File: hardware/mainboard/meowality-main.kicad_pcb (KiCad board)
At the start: 6 copper layers, 200 x 75 mm, 266 parts, among them J1 Micro_SD_Card_Det, J2 MINI_DP_SINK, J3 DEBUG, J4 USB_C_Receptacle, J5 Conn_01x02, J6 Conn_01x02, P1 M2_SOCKET_E, Q1 BSS138, Q10 BSS138, Q2 BSS138, Q3 BSS138, Q5 BSS138, Q7 BSS138, SW1 SW_DIP_x04, SW2 SW_Push, SW3 SW_Push, SW4 SW_Push, SW5 SW_Push, SW6 SW_Push, U1 CP3225-100.000-3.3-25-X-T-TR, U10 MMC5983MA, U11 Si52112-B, U12 TPD4E02B04DQA, U13 TPD4E02B04DQA, U14 CBTL02043A, U15 FUSB302B11MPX, U16 USB3318, U17 AP6230xWU, U19 ADP5070ACPZ, U2 AX3HAF1-135.0000T, U20 CAT4106HV4, U21 74LVC2T45DC, U3 AP6230xWU, U4 AP6230xWU, U5 SiC438, U6 AP6230xWU, U7 AP6230xWU, U8 TXS02612, U9 ICM-20789, X1 831056169, Y1 25MHz

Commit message: Fix LCD connector rotation
Signed-off-by: gatecat <gatecat@ds0.me>
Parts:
- turned LCD1 to 90 degrees
- turned LCD2 to 90 degrees

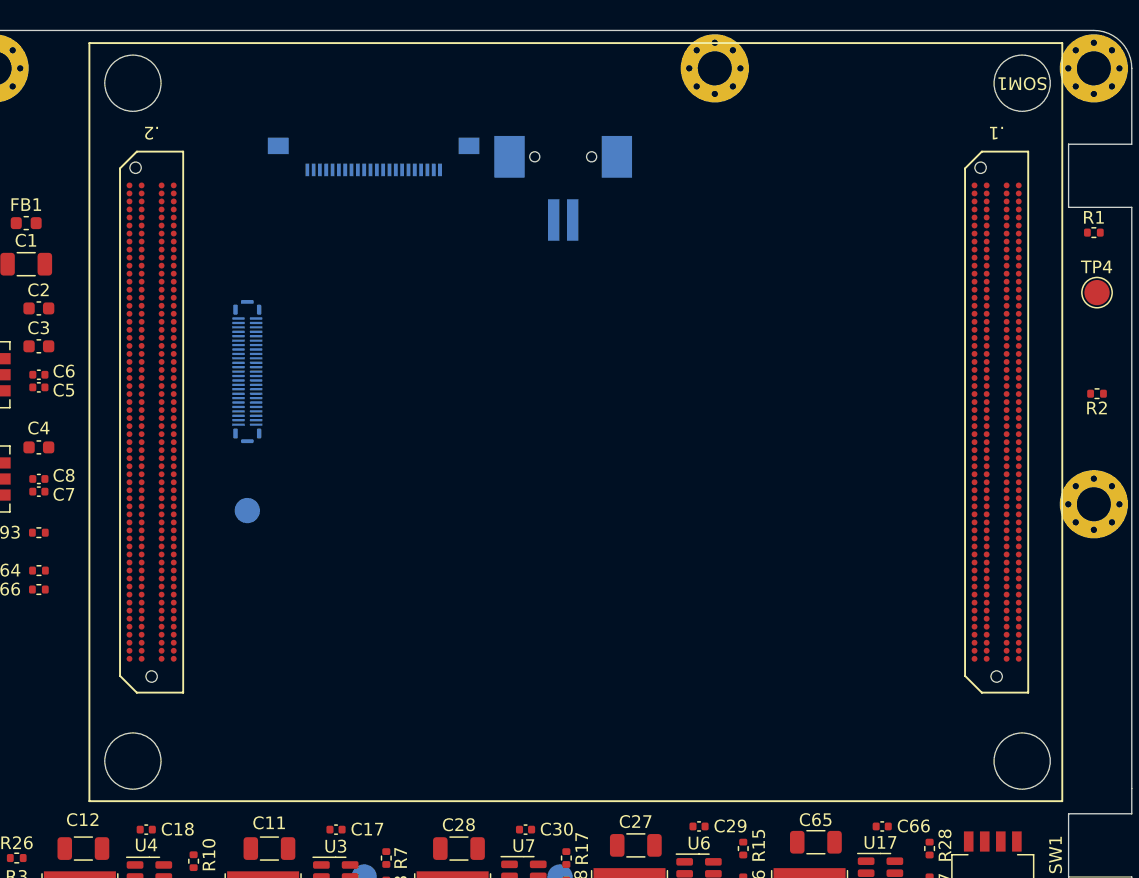
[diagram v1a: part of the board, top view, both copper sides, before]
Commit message: Minor layout changes
Signed-off-by: gatecat <gatecat@ds0.me>
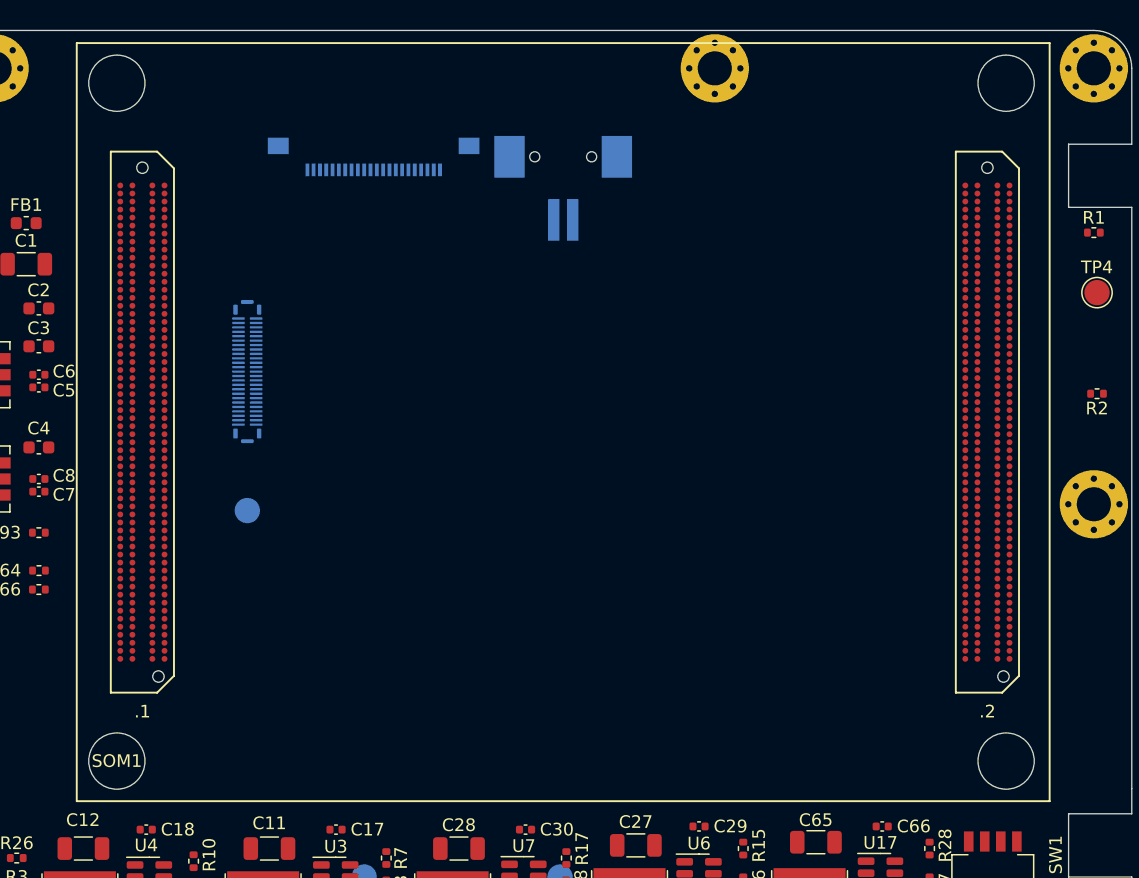
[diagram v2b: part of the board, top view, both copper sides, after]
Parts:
- moved SOM1 89.5 mm to (149.7, 117.8), turned to 0 degrees

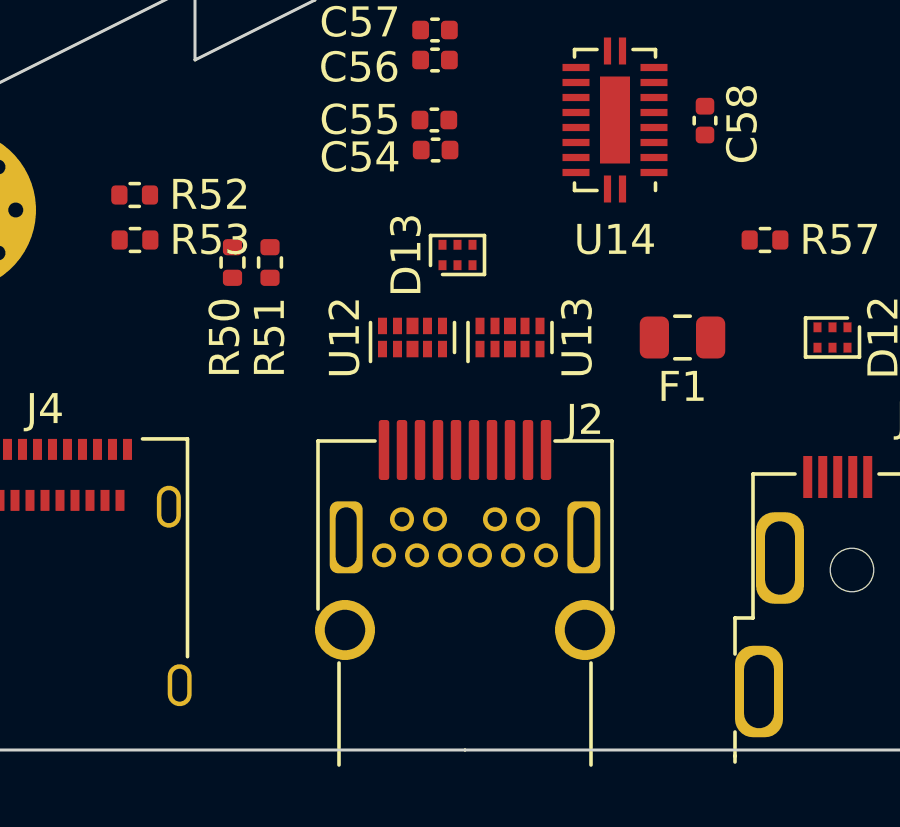
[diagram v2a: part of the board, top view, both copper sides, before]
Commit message: Alternate DP connector
Signed-off-by: gatecat <gatecat@ds0.me>
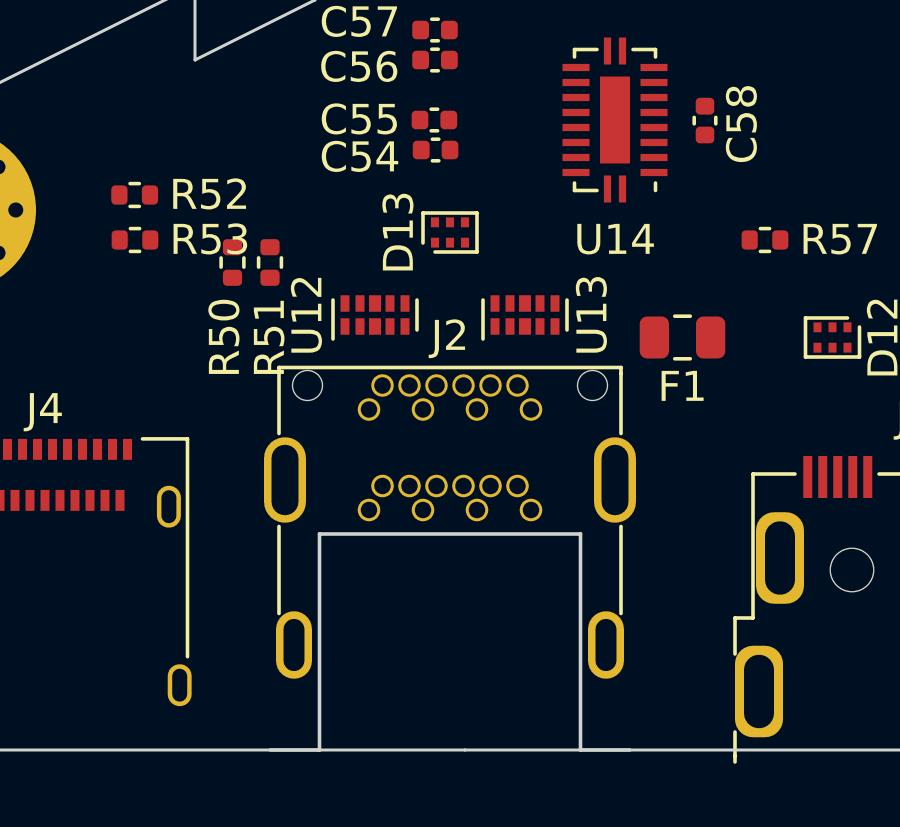
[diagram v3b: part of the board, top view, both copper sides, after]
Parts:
- J2: footprint meowality:E9320-001-01 -> meowality:2129320-3
- moved J2 8.17 mm to (49.5, 122.8), turned to 0 degrees
- moved U12 1.46 mm to (47.0, 120.5)
- moved U13 0.90 mm to (52.0, 120.5)
- moved D13 0.79 mm to (49.5, 117.8)
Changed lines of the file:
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@@
     )
   )
-  (footprint "meowality:E9320-001-01" (layer "F.Cu")
-    (at 50 131 180)
+  (footprint "meowality:2129320-3" (layer "F.Cu")
+    (at 49.5 122.85)
     (property "Sheetfile" "io.kicad_sch")
     (property "Sheetname" "IO")
-    (attr smd)
-    (fp_text reference "J2" (at -4 7 unlocked) (layer "F.SilkS")
+    (attr through_hole)
+    (fp_text reference "J2" (at 0 -1.65 unlocked) (layer "F.SilkS")
       (effects (font (size 1 1) (thickness 0.15)))
     )
-    (fp_text value "MINI_DP_SINK" (at 0 1 180 unlocked) (layer "F.Fab")
+    (fp_text value "MINI_DP_SINK" (at 0 3.75 unlocked) (layer "F.Fab")
       (effects (font (size 1 1) (thickness 0.15)))
     )
-    (fp_text user "${REFERENCE}" (at 0 2.5 180 unlocked) (layer "F.Fab")
+    (fp_text user "${REFERENCE}" (at 0 2.5 unlocked) (layer "F.Fab")
       (effects (font (size 1 1) (thickness 0.15)))
     )
-    (fp_line (start 4.9 6.3) (end 4.9 0.7) (layer "F.SilkS") (width 0.12))
-    (fp_line (start -4.9 6.3) (end -3 6.3) (layer "F.SilkS") (width 0.12))
-    (fp_line (start -4.2 -1.1) (end -4.2 -4.5) (layer "F.SilkS") (width 0.12))
-    (fp_line (start -4.9 0.7) (end -4.9 6.3) (layer "F.SilkS") (width 0.12))
-    (fp_line (start 4.2 -4.5) (end 4.2 -1.1) (layer "F.SilkS") (width 0.12))
-    (fp_line (start 3 6.3) (end 4.9 6.3) (layer "F.SilkS") (width 0.12))
-    (fp_line (start 0 -4.5) (end 4.2 -4.5) (layer "Eco1.User") (width 0.12))
-    (fp_line (start 0 -4.5) (end -4.2 -4.5) (layer "Eco1.User") (width 0.12))
-    (pad "1" smd roundrect (at 2.7 6 180) (size 0.35 2) (layers "F.Cu" "F.Paste" "F.Mask") (roundrect_rratio 0.25)
+    (fp_line (start 5.7 -0.4) (end 5.7 1.6) (layer "F.SilkS") (width 0.12))
+    (fp_line (start 5.7 -0.6) (end -5.7 -0.6) (layer "F.SilkS") (width 0.12))
+    (fp_line (start -5.7 -0.6) (end -5.7 1.6) (layer "F.SilkS") (width 0.12))
+    (fp_line (start 5.7 -0.4) (end 5.7 -0.6) (layer "F.SilkS") (width 0.12))
+    (fp_line (start 5.7 4.7) (end 5.7 7.6) (layer "F.SilkS") (width 0.12))
+    (fp_line (start -5.7 4.7) (end -5.7 7.6) (layer "F.SilkS") (width 0.12))
+    (fp_line (start 4.35 4.95) (end -4.35 4.95) (layer "Edge.Cuts") (width 0.12))
+    (fp_line (start 4.35 12.15) (end 6 12.15) (layer "Edge.Cuts") (width 0.12))
+    (fp_line (start -4.35 4.95) (end -4.35 12.15) (layer "Edge.Cuts") (width 0.12))
+    (fp_line (start 4.35 12.15) (end 4.35 4.95) (layer "Edge.Cuts") (width 0.12))
+    (fp_line (start -4.35 12.15) (end -6 12.15) (layer "Edge.Cuts") (width 0.12))
+    (pad "" np_thru_hole circle (at -4.75 0) (size 1 1) (drill 1) (layers F&B.Cu *.Mask))
+    (pad "" np_thru_hole circle (at 4.75 0) (size 1 1) (drill 1) (layers F&B.Cu *.Mask))
+    (pad "1" thru_hole circle (at -2.7 4.15) (size 0.75 0.75) (drill 0.55) (layers *.Cu *.Mask)
       (net 2 "GND") (pinfunction "GND") (pintype "passive"))
-    (pad "2" thru_hole circle (at 2.7 2.49 180) (size 0.8 0.8) (drill 0.5) (layers *.Cu "B.Mask")
+    (pad "2" thru_hole circle (at -2.7 0.8) (size 0.75 0.75) (drill 0.55) (layers *.Cu *.Mask)
       (net 111 "DP_HPD") (pinfunction "HPD") (pintype "passive"))
-    (pad "3" smd roundrect (at 2.1 6 180) (size 0.35 2) (layers "F.Cu" "F.Paste" "F.Mask") (roundrect_rratio 0.25)
+    (pad "3" thru_hole circle (at -2.25 3.35) (size 0.75 0.75) (drill 0.55) (layers *.Cu *.Mask)
       (net 129 "DP_IN_L3-") (pinfunction "ML_L3-") (pintype "passive"))
-    (pad "4" thru_hole circle (at 2.1 3.69 180) (size 0.8 0.8) (drill 0.5) (layers *.Cu "B.Mask")
+    (pad "4" thru_hole circle (at -2.25 0) (size 0.75 0.75) (drill 0.55) (layers *.Cu *.Mask)
       (net 130 "Net-(J2-Pad4)") (pinfunction "CONFIG1") (pintype "passive"))
-    (pad "5" smd roundrect (at 1.5 6 180) (size 0.35 2) (layers "F.Cu" "F.Paste" "F.Mask") (roundrect_rratio 0.25)
+    (pad "5" thru_hole circle (at -1.35 3.35) (size 0.75 0.75) (drill 0.55) (layers *.Cu *.Mask)
       (net 131 "DP_IN_L3+") (pinfunction "ML_L3+") (pintype "passive"))
-    (pad "6" thru_hole circle (at 1.6 2.49 180) (size 0.8 0.8) (drill 0.5) (layers *.Cu "B.Mask")
+    (pad "6" thru_hole circle (at -1.35 0) (size 0.75 0.75) (drill 0.55) (layers *.Cu *.Mask)
       (net 132 "Net-(J2-Pad6)") (pinfunction "CONFIG2") (pintype "passive"))
-    (pad "7" smd roundrect (at 0.9 6 180) (size 0.35 2) (layers "F.Cu" "F.Paste" "F.Mask") (roundrect_rratio 0.25)
+    (pad "7" thru_hole circle (at -0.9 4.15) (size 0.75 0.75) (drill 0.55) (layers *.Cu *.Mask)
       (net 2 "GND") (pinfunction "GND") (pintype "passive"))
-    (pad "8" thru_hole circle (at 1 3.69 180) (size 0.8 0.8) (drill 0.5) (layers *.Cu "B.Mask")
+    (pad "8" thru_hole circle (at -0.9 0.8) (size 0.75 0.75) (drill 0.55) (layers *.Cu *.Mask)
       (net 2 "GND") (pinfunction "GND") (pintype "passive"))
-    (pad "9" smd roundrect (at 0.3 6 180) (size 0.35 2) (layers "F.Cu" "F.Paste" "F.Mask") (roundrect_rratio 0.25)
+    (pad "9" thru_hole circle (at -0.45 3.35) (size 0.75 0.75) (drill 0.55) (layers *.Cu *.Mask)
       (net 133 "DP_IN_L2-") (pinfunction "ML_L2-") (pintype "passive"))
-    (pad "10" thru_hole circle (at 0.5 2.49 180) (size 0.8 0.8) (drill 0.5) (layers *.Cu "B.Mask")
+    (pad "10" thru_hole circle (at -0.45 0) (size 0.75 0.75) (drill 0.55) (layers *.Cu *.Mask)
       (net 134 "DP_IN_L0-") (pinfunction "ML_L0-") (pintype "passive"))
-    (pad "11" smd roundrect (at -0.3 6 180) (size 0.35 2) (layers "F.Cu" "F.Paste" "F.Mask") (roundrect_rratio 0.25)
+    (pad "11" thru_hole circle (at 0.45 3.35) (size 0.75 0.75) (drill 0.55) (layers *.Cu *.Mask)
       (net 135 "DP_IN_L2+") (pinfunction "ML_L2+") (pintype "passive"))
-    (pad "12" thru_hole circle (at -0.5 2.49 180) (size 0.8 0.8) (drill 0.5) (layers *.Cu "B.Mask")
+    (pad "12" thru_hole circle (at 0.45 0) (size 0.75 0.75) (drill 0.55) (layers *.Cu *.Mask)
       (net 136 "DP_IN_L0+") (pinfunction "ML_L0+") (pintype "passive"))
-    (pad "13" smd roundrect (at -0.9 6 180) (size 0.35 2) (layers "F.Cu" "F.Paste" "F.Mask") (roundrect_rratio 0.25)
+    (pad "13" thru_hole circle (at 0.9 4.15) (size 0.75 0.75) (drill 0.55) (layers *.Cu *.Mask)
       (net 2 "GND") (pinfunction "GND") (pintype "passive"))
-    (pad "14" thru_hole circle (at -1 3.69 180) (size 0.8 0.8) (drill 0.5) (layers *.Cu "B.Mask")
+    (pad "14" thru_hole circle (at 0.9 0.8) (size 0.75 0.75) (drill 0.55) (layers *.Cu *.Mask)
       (net 2 "GND") (pinfunction "GND") (pintype "passive"))
-    (pad "15" smd roundrect (at -1.5 6 180) (size 0.35 2) (layers "F.Cu" "F.Paste" "F.Mask") (roundrect_rratio 0.25)
+    (pad "15" thru_hole circle (at 1.35 3.35) (size 0.75 0.75) (drill 0.55) (layers *.Cu *.Mask)
       (net 137 "DP_IN_L1-") (pinfunction "ML_L1-") (pintype "passive"))
-    (pad "16" thru_hole circle (at -1.6 2.49 180) (size 0.8 0.8) (drill 0.5) (layers *.Cu "B.Mask")
+    (pad "16" thru_hole circle (at 1.35 0) (size 0.75 0.75) (drill 0.55) (layers *.Cu *.Mask)
       (net 112 "DP_AUX+") (pinfunction "AUX+") (pintype "passive"))
-    (pad "17" smd roundrect (at -2.1 6 180) (size 0.35 2) (layers "F.Cu" "F.Paste" "F.Mask") (roundrect_rratio 0.25)
+    (pad "17" thru_hole circle (at 2.25 3.35) (size 0.75 0.75) (drill 0.55) (layers *.Cu *.Mask)
       (net 138 "DP_IN_L1+") (pinfunction "ML_L1+") (pintype "passive"))
-    (pad "18" thru_hole circle (at -2.1 3.69 180) (size 0.8 0.8) (drill 0.5) (layers *.Cu *.Mask)
+    (pad "18" thru_hole circle (at 2.25 0) (size 0.75 0.75) (drill 0.55) (layers *.Cu *.Mask)
       (net 113 "DP_AUX-") (pinfunction "AUX-") (pintype "passive"))
-    (pad "19" smd roundrect (at -2.7 6 180) (size 0.35 2) (layers "F.Cu" "F.Paste" "F.Mask") (roundrect_rratio 0.25)
+    (pad "19" thru_hole circle (at 2.7 4.15) (size 0.75 0.75) (drill 0.55) (layers *.Cu *.Mask)
       (net 2 "GND") (pinfunction "GND") (pintype "passive"))
-    (pad "20" thru_hole circle (at -2.7 2.49 180) (size 0.8 0.8) (drill 0.5) (layers *.Cu *.Mask)
+    (pad "20" thru_hole circle (at 2.7 0.8) (size 0.75 0.75) (drill 0.55) (layers *.Cu *.Mask)
       (net 121 "Net-(F1-Pad2)") (pinfunction "DP_PWR") (pintype "passive"))
-    (pad "S" thru_hole circle (at 4 0 180) (size 2 2) (drill 1.35) (layers *.Cu *.Mask)
+    (pad "S" thru_hole oval (at 5.5 3.15) (size 1.4 2.85) (drill oval 0.9 2.35) (layers *.Cu *.Mask)
       (net 2 "GND") (pintype "passive"))
-    (pad "S" thru_hole roundrect (at 3.96 3.09 180) (size 1.1 2.4) (drill oval 0.7 2) (layers *.Cu *.Mask) (roundrect_rratio 0.25)
+    (pad "S" thru_hole oval (at -5.2 8.65) (size 1.2 2.25) (drill oval 0.7 1.74) (layers *.Cu *.Mask)
       (net 2 "GND") (pintype "passive"))
-    (pad "S" thru_hole circle (at -4 0 180) (size 2 2) (drill 1.35) (layers *.Cu *.Mask)
+    (pad "S" thru_hole oval (at 5.2 8.65) (size 1.2 2.25) (drill oval 0.7 1.74) (layers *.Cu *.Mask)
       (net 2 "GND") (pintype "passive"))
-    (pad "S" thru_hole roundrect (at -3.96 3.09 180) (size 1.1 2.4) (drill oval 0.7 2) (layers *.Cu *.Mask) (roundrect_rratio 0.25)
+    (pad "S" thru_hole oval (at -5.5 3.15) (size 1.4 2.85) (drill oval 0.9 2.35) (layers *.Cu *.Mask)
       (net 2 "GND") (pintype "passive"))
   )
@@
   )
   (footprint "Package_SON:USON-10_2.5x1.0mm_P0.5mm" (layer "F.Cu")
-    (at 48.25 121.25 90)
+    (at 47 120.5 90)
     (descr "USON-10 2.5x1.0mm_ Pitch 0.5mm http://www.ti.com/lit/ds/symlink/tpd4e02b04.pdf")
     (tags "USON-10 2.5x1.0mm Pitch 0.5mm")
@@
   )
   (footprint "Package_TO_SOT_SMD:SOT-886" (layer "F.Cu")
-    (at 49.75 118.5 90)
+    (at 49.5 117.75 90)
     (descr "SOT-886")
     (tags "SOT-886")
@@
   )
   (footprint "Package_SON:USON-10_2.5x1.0mm_P0.5mm" (layer "F.Cu")
-    (at 51.5 121.25 90)
+    (at 52 120.5 90)
     (descr "USON-10 2.5x1.0mm_ Pitch 0.5mm http://www.ti.com/lit/ds/symlink/tpd4e02b04.pdf")
     (tags "USON-10 2.5x1.0mm Pitch 0.5mm")
